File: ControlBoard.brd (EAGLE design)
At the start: 160 x 100 mm, 2 parts, among them J1 47053-1000, U1 ARDUINO_PRO_MINI

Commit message: Made the first version of the pcb
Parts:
- removed J1: 47053-1000, 47053-1000:470531000
- removed U1: ARDUINO_PRO_MINI, ARDUINO_PRO_MINI:MODULE_ARDUINO_PRO_MINI
- added 12VBATTERY, PELTIER: B2B-XH-A(LF)(SN), B2B-XH-A_LF__SN_:JST_B2B-XH-A(LF)(SN)
- added ARDUINO-NANO: ABX00028, ABX00028:MODULE_ABX00028
- added FAN: 47053-1000, 47053-1000:470531000
- added ICMOSFET: RFP30N06LE, RFP30N06LE:TRANS_RFP30N06LE
- added ICOPAMP: LM358, LM358:DIP08
- added R1: 1Ω, adafruit:0805-THM
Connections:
- removed net GND_1: U1.JP6_2
- removed net GND_2: U1.JP7_9
- removed net RAW: U1.JP6_1
- removed net VCC: U1.JP1_4
- removed net VCC_1: U1.JP6_4
- new net +3V3: ARDUINO-NANO.2
- new net +5V: ARDUINO-NANO.12
- new net IREGULATOR: ICMOSFET.2, PELTIER.2
- new net N$1: ICMOSFET.3, ICOPAMP.2, R1.1
- new net N$5: ICMOSFET.1, ICOPAMP.1
- new net PELTIERCONTROL: ARDUINO-NANO.5, ICOPAMP.3
- net 12V: now also 12VBATTERY.1, ARDUINO-NANO.15, FAN.2, PELTIER.1; no longer J1.2
- net GND: now also 12VBATTERY.2, ARDUINO-NANO.14, ARDUINO-NANO.19, FAN.1, R1.2; no longer J1.1, U1.JP1_5, U1.JP1_6
- net N$3: now also FAN.3; no longer J1.3
- net PWM: now also ARDUINO-NANO.21, FAN.4; no longer J1.4, U1.JP7_7
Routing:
- net PWM: track 0.00 -> 64.8 mm
- net GND: track 0.00 -> 59.3 mm
- net 12V: track 0.00 -> 52.1 mm
- net N$1: track 0.00 -> 14.5 mm
- net PELTIERCONTROL: track 0.00 -> 11.0 mm
- net IREGULATOR: track 0.00 -> 10.2 mm
- net N$5: track 0.00 -> 10.2 mm
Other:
- board size 160 x 100 mm -> 47 x 61.9 mm
- board text added: "+"
- board text added: "-"

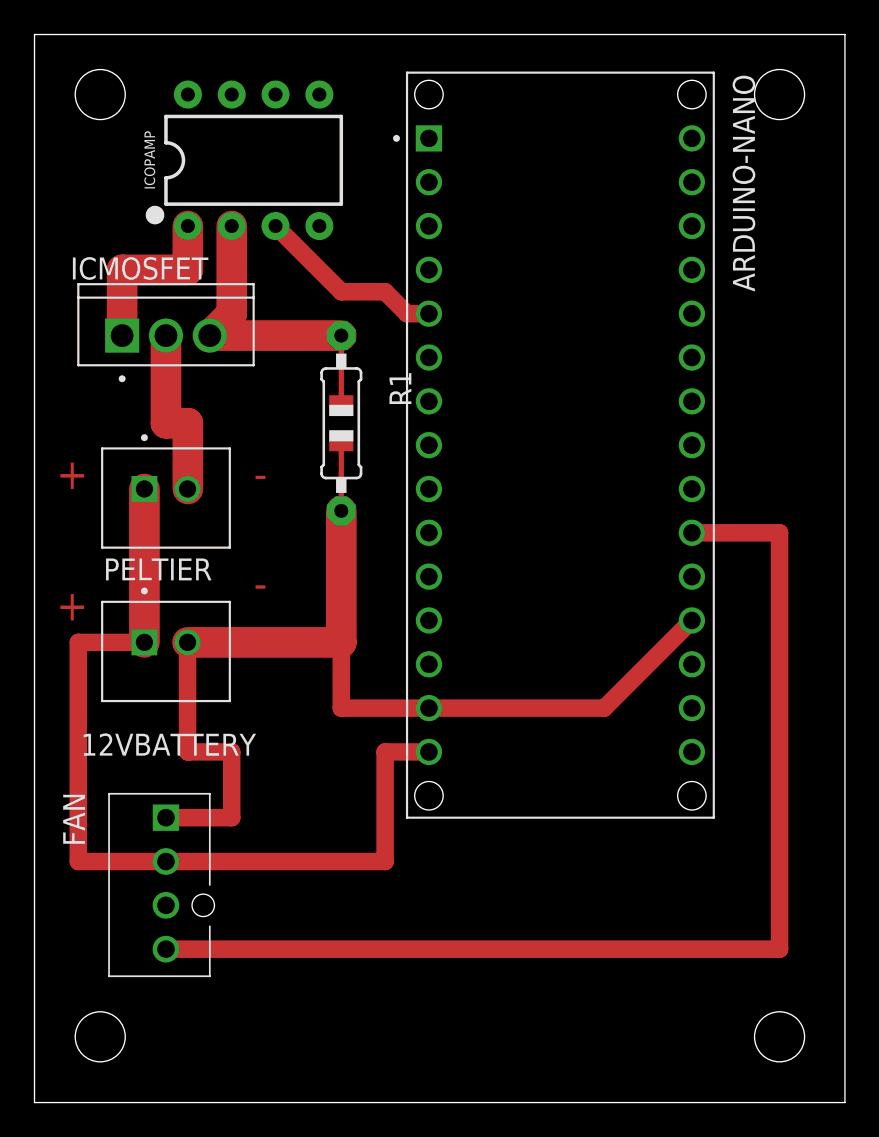
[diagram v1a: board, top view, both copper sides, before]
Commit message: Cleaned a bit of the pcb and addded the tmp36 thermocouple
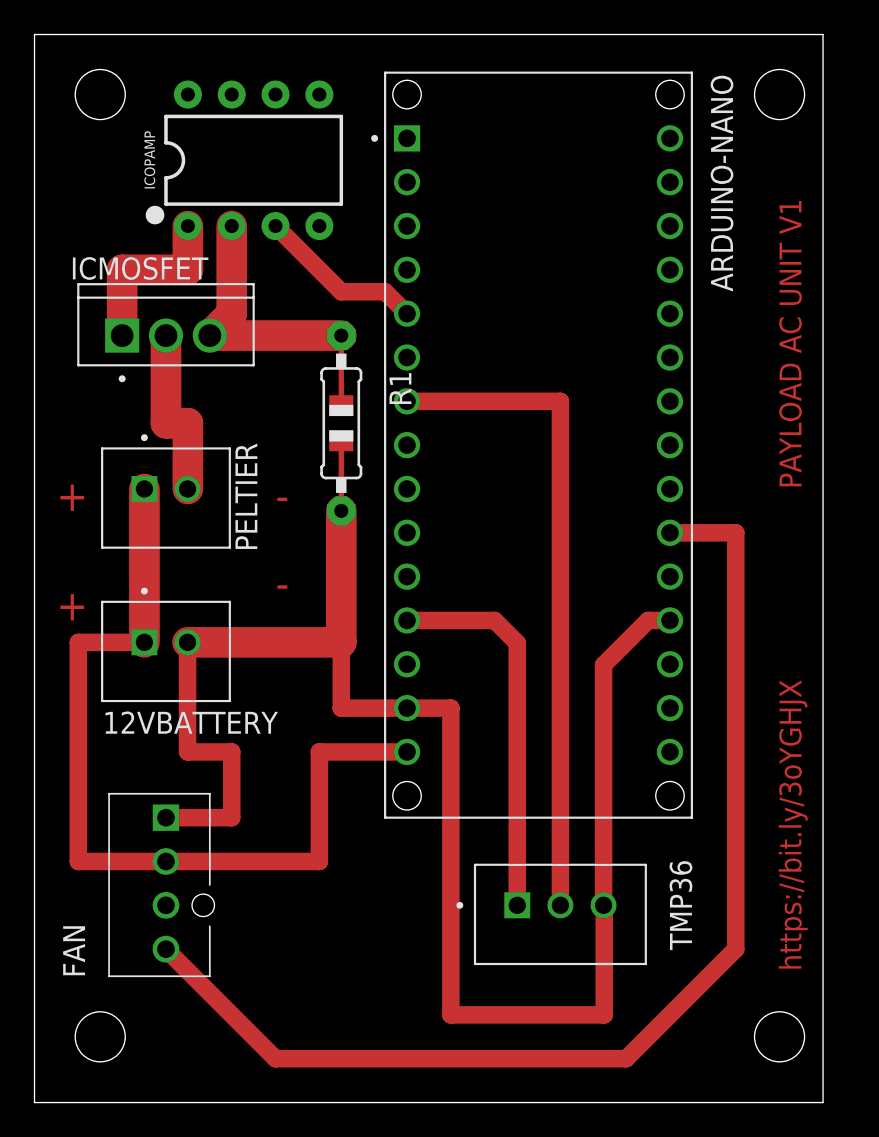
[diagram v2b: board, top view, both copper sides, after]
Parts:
- added TMP36: B3B-XH-A(LF)(SN), B3B-XH-A_LF__SN_:JST_B3B-XH-A(LF)(SN)
- moved ARDUINO-NANO 1.27 mm to (29.2, 38.1)
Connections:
- removed net +5V: ARDUINO-NANO.12
- new net 5V: ARDUINO-NANO.12, TMP36.1
- new net THERMOCOUPLE: ARDUINO-NANO.7, TMP36.2
- net GND: now also TMP36.3
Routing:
- net THERMOCOUPLE: track 0.00 -> 38.1 mm
- net GND: track 59.3 -> 95.1 mm
- net 5V: track 0.00 -> 22.1 mm
- net PWM: track 64.8 -> 66.2 mm
- net 12V: track 52.1 -> 50.8 mm
- net PELTIERCONTROL: track 11.0 -> 9.72 mm
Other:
- board size 47 x 61.9 mm -> 45.7 x 61.9 mm
- board text added: "PAYLOAD AC UNIT V1"
- board text added: "https://bit.ly/3oYGHJX"

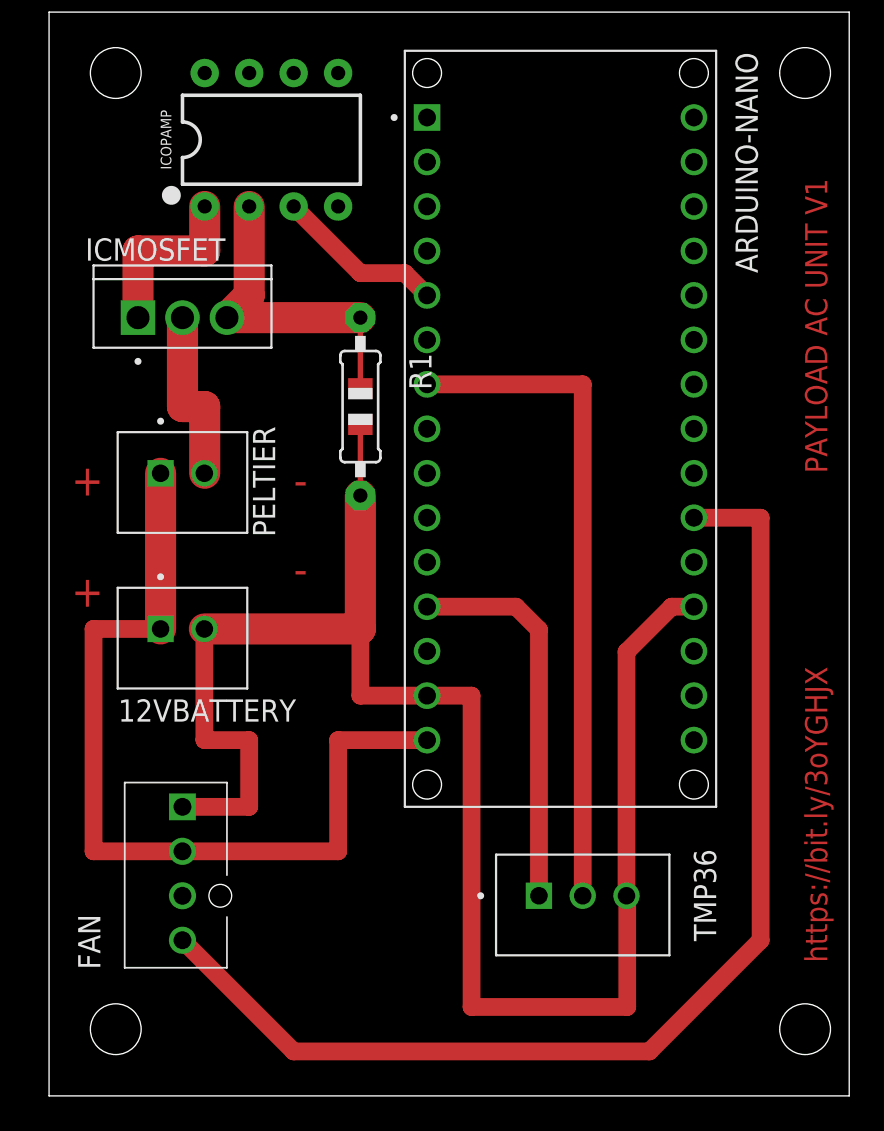
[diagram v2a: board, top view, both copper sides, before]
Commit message: Moved all traces to the bottom layer to allow for othermill pro manufacturing
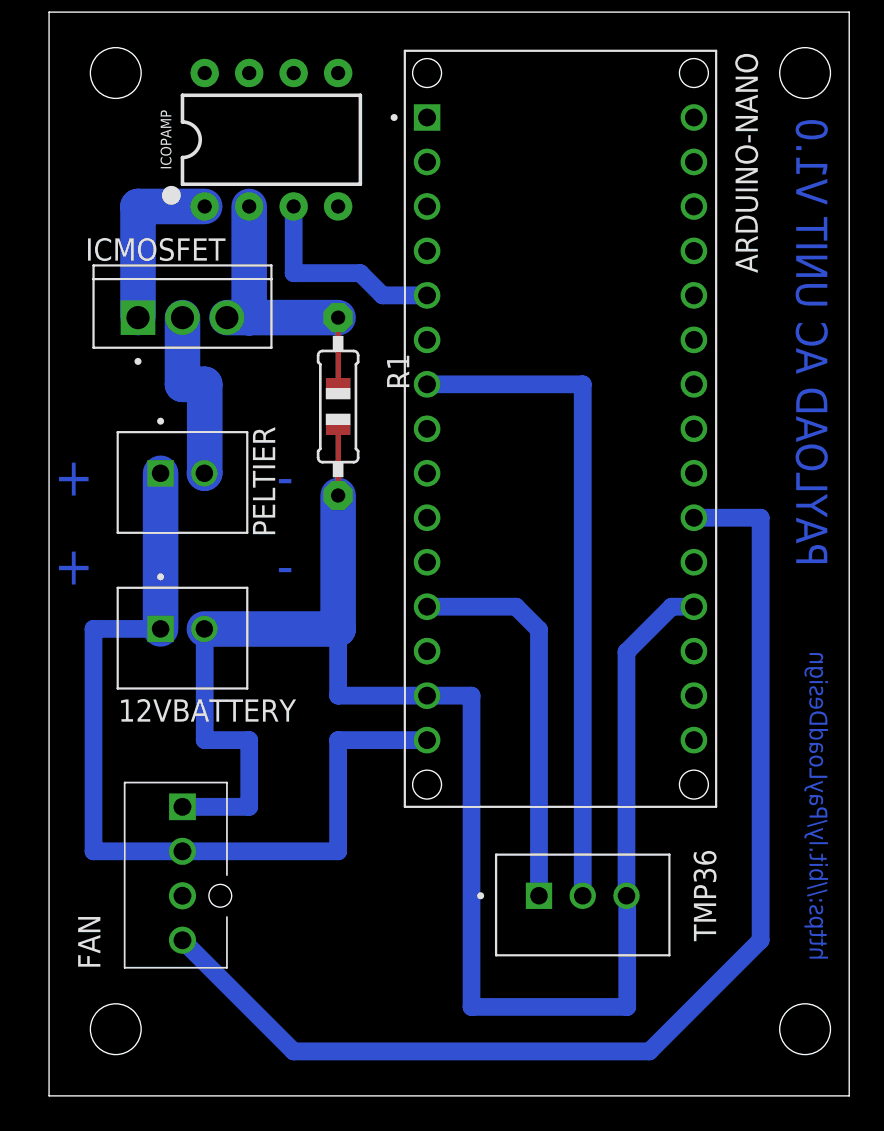
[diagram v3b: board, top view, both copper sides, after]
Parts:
- moved R1 1.27 mm to (16.5, 39.4)
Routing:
- net PELTIERCONTROL: track 9.72 -> 12.0 mm
- net N$1: track 14.5 -> 12.7 mm
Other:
- board text added: "PAYLOAD AC UNIT V1.0"
- board text added: "https://bit.ly/PayLoadDesign"
- board text removed: "PAYLOAD AC UNIT V1"
- board text removed: "https://bit.ly/3oYGHJX"
